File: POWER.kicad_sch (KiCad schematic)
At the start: 44 parts, among them U1 LMR604303SRAKRQ1, U21 LMR43620R5RPER, U22 AP7361C-33FGE-7, U23 AP7361C-33FGE-7

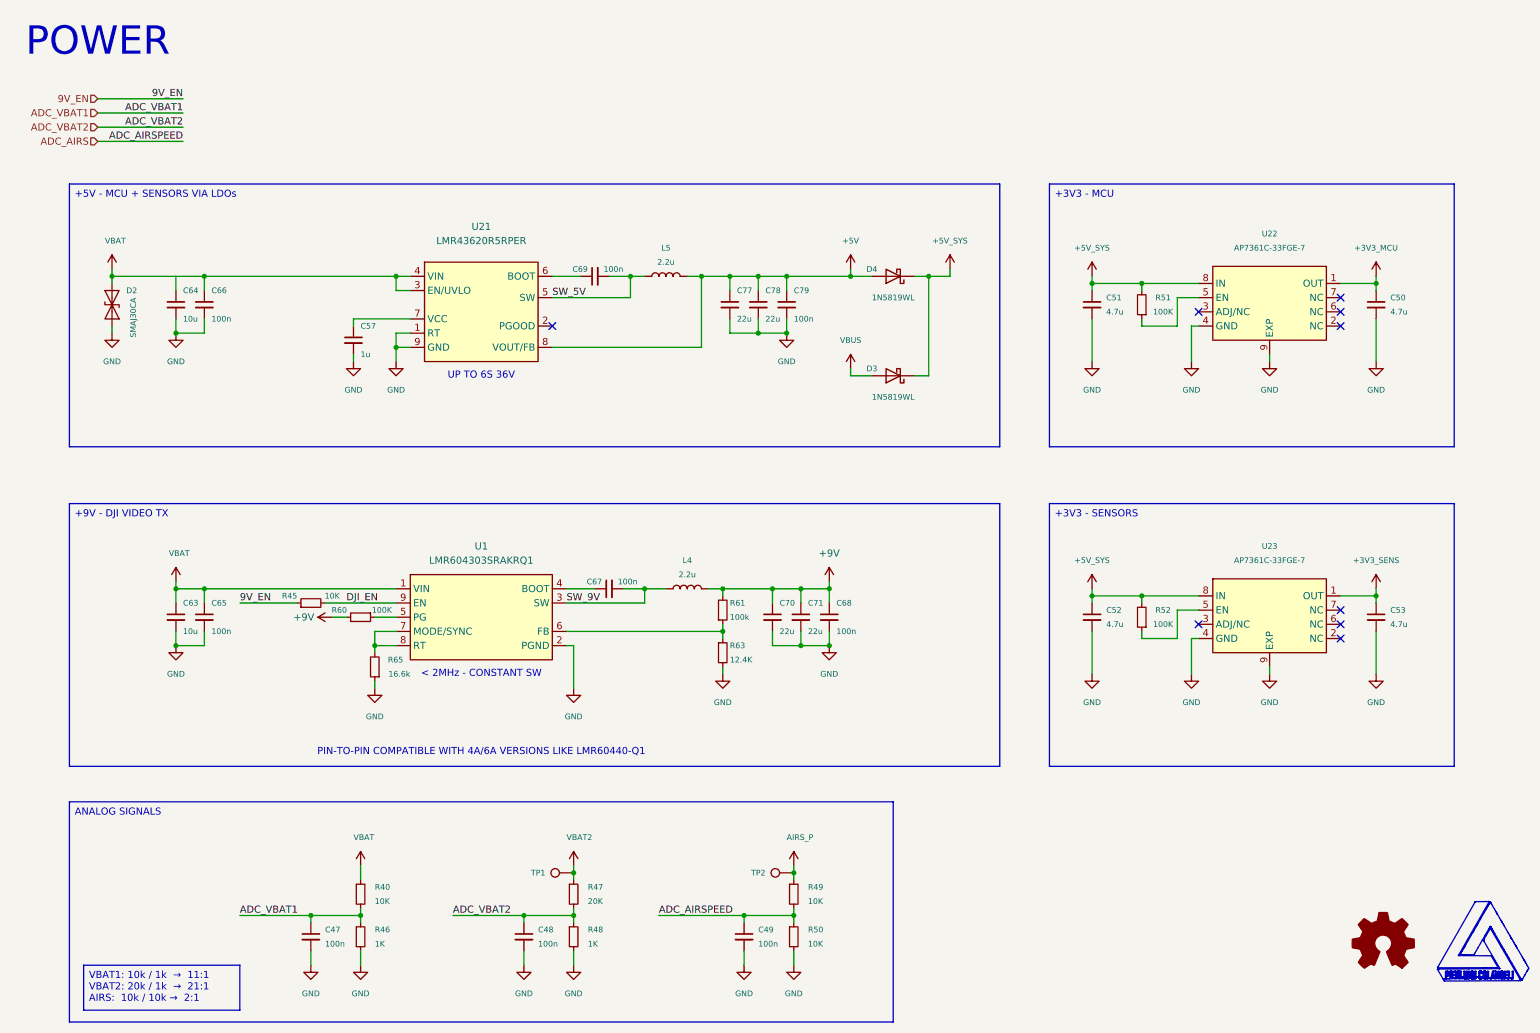
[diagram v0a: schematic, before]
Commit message: grouped ICs and passives
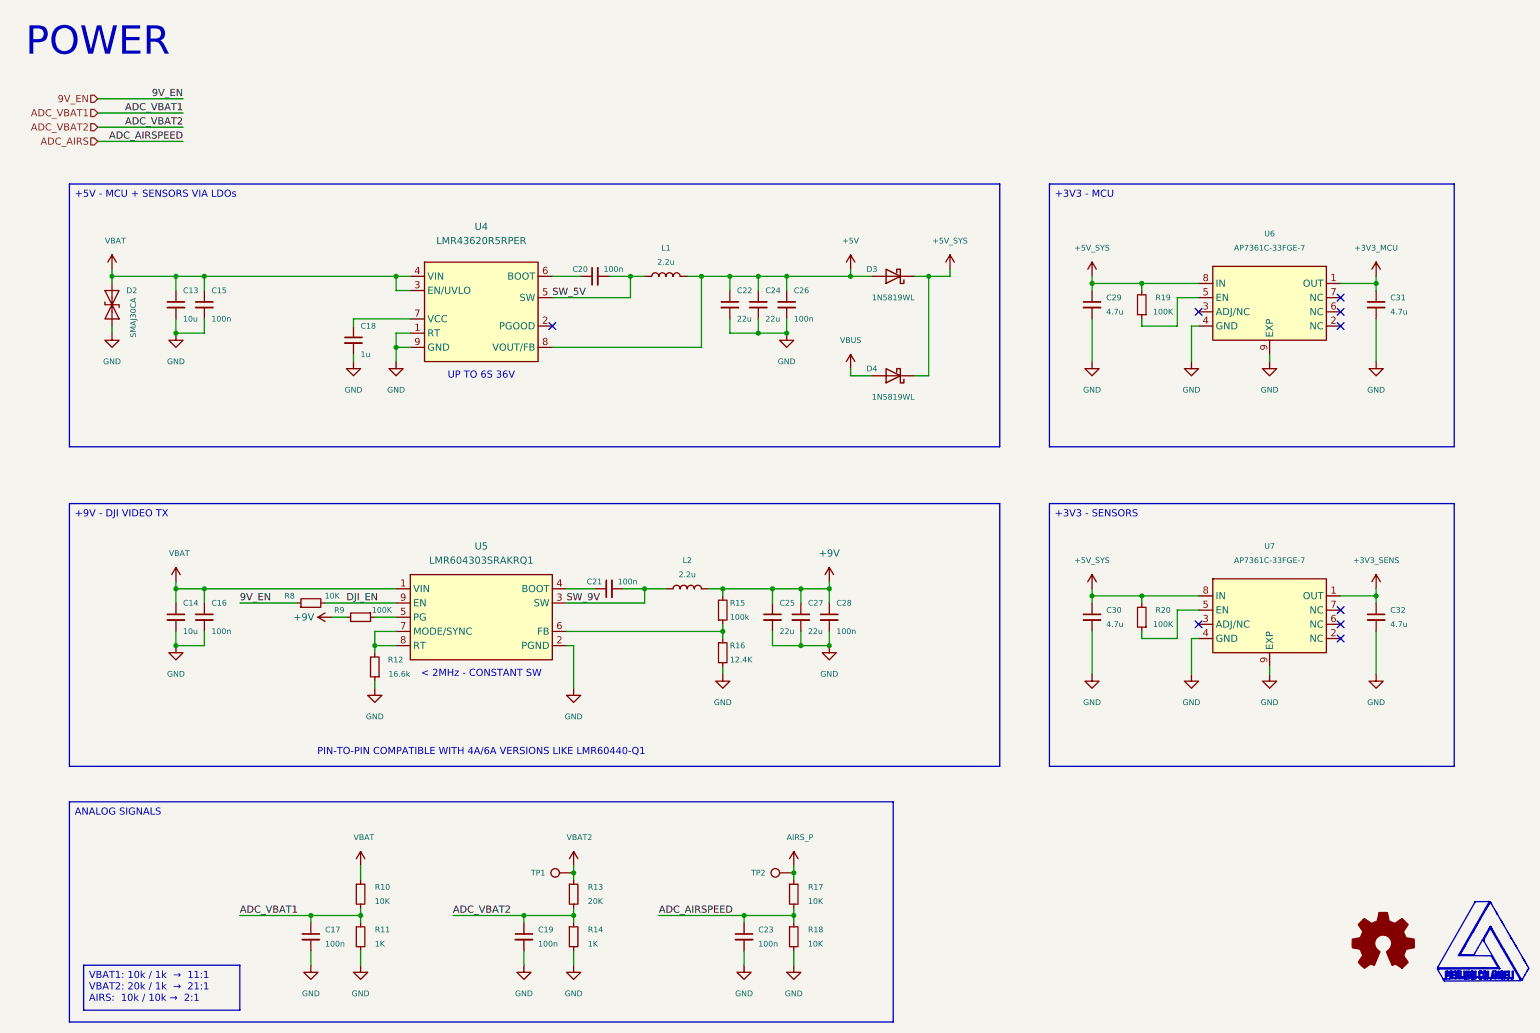
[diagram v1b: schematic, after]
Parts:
- renumbered C64 to C13, C63 to C14, C66 to C15, C65 to C16, C47 to C17, C57 to C18, C48 to C19, C69 to C20, C67 to C21, C77 to C22, C49 to C23, C78 to C24, C70 to C25, C79 to C26, C71 to C27, C68 to C28, C51 to C29, C52 to C30, C50 to C31, C53 to C32, D4 to D3, D3 to D4, L5 to L1, L4 to L2, R40 to R10, R46 to R11, R65 to R12, R47 to R13, R48 to R14, R61 to R15, R63 to R16, R49 to R17, R50 to R18, R51 to R19, R52 to R20, R45 to R8, R60 to R9, U21 to U4, U1 to U5, U22 to U6, U23 to U7
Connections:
- net VBAT: now also C13.1
